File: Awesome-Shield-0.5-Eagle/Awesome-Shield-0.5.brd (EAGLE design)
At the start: 100 x 80 mm, 24 parts, among them J1 ARDUINO_R3_SHIELDUNO_R3_SHIEL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, SW1 SPST_TACT-EVQQ2

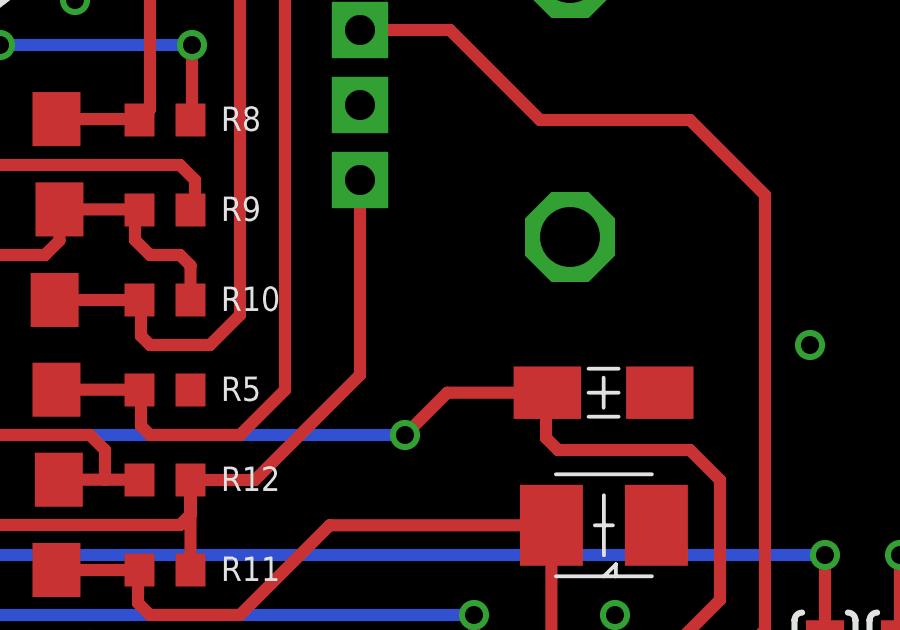
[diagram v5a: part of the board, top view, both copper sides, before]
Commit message: changed vias to round
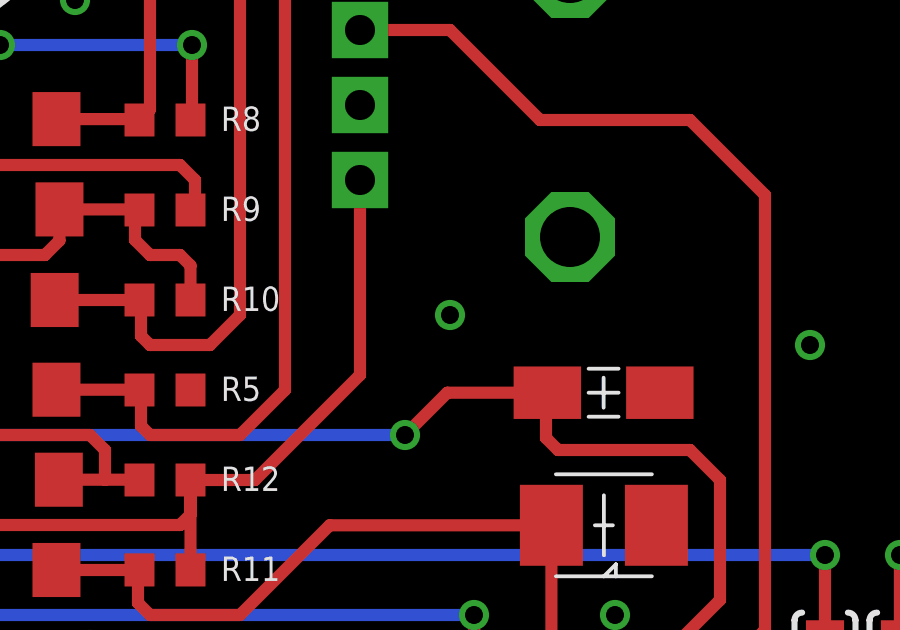
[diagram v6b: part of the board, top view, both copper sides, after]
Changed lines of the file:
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@@
 <vertex x="81.3" y="71.1"/>
 </polygon>
-<via x="32.5" y="57" extent="1-16" drill="0.6" shape="square"/>
-<via x="78.5" y="35.5" extent="1-16" drill="0.6" shape="square"/>
-<via x="38.5" y="21.5" extent="1-16" drill="0.6" shape="square"/>
-<via x="54" y="47" extent="1-16" drill="0.6" shape="square"/>
-<via x="82" y="52.5" extent="1-16" drill="0.6" shape="square"/>
-<via x="72" y="26.5" extent="1-16" drill="0.6" shape="square"/>
-<wire x1="73.495" y1="33.91" x2="73.38" y2="29.49" width="0" layer="19" extent="1-1"/>
+<via x="32.5" y="57" extent="1-16" drill="0.6"/>
+<via x="78.5" y="35.5" extent="1-16" drill="0.6"/>
+<via x="38.5" y="21.5" extent="1-16" drill="0.6"/>
+<via x="54" y="47" extent="1-16" drill="0.6"/>
+<via x="82" y="52.5" extent="1-16" drill="0.6"/>
+<via x="72" y="26.5" extent="1-16" drill="0.6"/>
+<via x="66.5" y="36.5" extent="1-16" drill="0.6"/>
 </signal>
 <signal name="A2">
@@
 <wire x1="69.745" y1="33.91" x2="66.41" y2="33.91" width="0.4064" layer="1"/>
 <wire x1="66.41" y1="33.91" x2="65" y2="32.5" width="0.4064" layer="1"/>
-<via x="65" y="32.5" extent="1-16" drill="0.6" shape="square"/>
+<via x="65" y="32.5" extent="1-16" drill="0.6"/>
 <wire x1="65" y1="32.5" x2="48" y2="32.5" width="0.4064" layer="16"/>
-<via x="48" y="32.5" extent="1-16" drill="0.6" shape="square"/>
+<via x="48" y="32.5" extent="1-16" drill="0.6"/>
 <wire x1="48" y1="32.5" x2="54.5" y2="32.5" width="0.4064" layer="1"/>
 <wire x1="54.5" y1="32.5" x2="55" y2="32" width="0.4064" layer="1"/>
@@
 <wire x1="54.61" y1="20.066" x2="54.61" y2="25.39" width="0.4064" layer="1"/>
 <wire x1="54.61" y1="25.39" x2="54.5" y2="25.5" width="0.4064" layer="1"/>
-<via x="54.5" y="25.5" extent="1-16" drill="0.6" shape="square"/>
+<via x="54.5" y="25.5" extent="1-16" drill="0.6"/>
 <wire x1="54.5" y1="25.5" x2="41" y2="25.5" width="0.4064" layer="16"/>
 <wire x1="41" y1="25.5" x2="38" y2="28.5" width="0.4064" layer="16"/>
-<via x="38" y="28.5" extent="1-16" drill="0.6" shape="square"/>
+<via x="38" y="28.5" extent="1-16" drill="0.6"/>
 <wire x1="38" y1="28.5" x2="34.12" y2="28.5" width="0.4064" layer="1"/>
 <wire x1="34.12" y1="28.5" x2="34.06" y2="28.44" width="0.4064" layer="1"/>
@@
 <wire x1="67.31" y1="20.066" x2="67.31" y2="26.49" width="0.4064" layer="1"/>
 <wire x1="67.31" y1="26.49" x2="67.3" y2="26.5" width="0.4064" layer="1"/>
-<via x="67.3" y="26.5" extent="1-16" drill="0.6" shape="square"/>
+<via x="67.3" y="26.5" extent="1-16" drill="0.6"/>
 <wire x1="67.3" y1="26.5" x2="46.5" y2="26.5" width="0.4064" layer="16"/>
 <wire x1="46.5" y1="26.5" x2="46" y2="27" width="0.4064" layer="16"/>
-<via x="46" y="27" extent="1-16" drill="0.6" shape="square"/>
+<via x="46" y="27" extent="1-16" drill="0.6"/>
 <wire x1="46" y1="27" x2="46" y2="28.5" width="0.4064" layer="1"/>
 <wire x1="46" y1="28.5" x2="39.5" y2="35" width="0.4064" layer="1"/>
@@
 <contactref element="SJ2" pad="1"/>
 <wire x1="81.5" y1="26.008" x2="81.5" y2="28.5" width="0.4064" layer="1"/>
-<via x="81.5" y="28.5" extent="1-16" drill="0.6" shape="square"/>
+<via x="81.5" y="28.5" extent="1-16" drill="0.6"/>
 <wire x1="80" y1="24.5" x2="38" y2="24.5" width="0.4064" layer="16"/>
-<via x="38" y="24.5" extent="1-16" drill="0.6" shape="square"/>
+<via x="38" y="24.5" extent="1-16" drill="0.6"/>
 <wire x1="38" y1="24.5" x2="34.12" y2="24.5" width="0.4064" layer="1"/>
 <wire x1="34.12" y1="24.5" x2="34.06" y2="24.44" width="0.4064" layer="1"/>
@@
 <contactref element="SJ1" pad="1"/>
 <wire x1="79" y1="26.008" x2="79" y2="28.5" width="0.4064" layer="1"/>
-<via x="79" y="28.5" extent="1-16" drill="0.6" shape="square"/>
+<via x="79" y="28.5" extent="1-16" drill="0.6"/>
 <wire x1="79" y1="28.5" x2="42.5" y2="28.5" width="0.4064" layer="16"/>
-<via x="42.5" y="28.5" extent="1-16" drill="0.6" shape="square"/>
+<via x="42.5" y="28.5" extent="1-16" drill="0.6"/>
 <wire x1="42.5" y1="28.5" x2="40.5" y2="28.5" width="0.4064" layer="1"/>
 <wire x1="40.5" y1="28.5" x2="38.5" y2="26.5" width="0.4064" layer="1"/>
@@
 <wire x1="69.85" y1="68.58" x2="69.85" y2="66.15" width="0.4064" layer="1"/>
 <wire x1="69.85" y1="66.15" x2="70.5" y2="65.5" width="0.4064" layer="1"/>
-<via x="70.5" y="65.5" extent="1-16" drill="0.6" shape="square"/>
+<via x="70.5" y="65.5" extent="1-16" drill="0.6"/>
 <wire x1="70.5" y1="65.5" x2="61" y2="65.5" width="0.4064" layer="16"/>
 <wire x1="61" y1="65.5" x2="37.3" y2="41.8" width="0.4064" layer="16"/>
-<via x="37.3" y="41.8" extent="1-16" drill="0.6" shape="square"/>
+<via x="37.3" y="41.8" extent="1-16" drill="0.6"/>
 <wire x1="37.3" y1="41.8" x2="34.14" y2="41.8" width="0.4064" layer="1"/>
 <wire x1="34.14" y1="41.8" x2="34.06" y2="41.72" width="0.4064" layer="1"/>
@@
 <wire x1="50.538" y1="43.03" x2="50.538" y2="44.538" width="0.4064" layer="1"/>
 <wire x1="50.538" y1="44.538" x2="51.5" y2="45.5" width="0.4064" layer="1"/>
-<via x="51.5" y="45.5" extent="1-16" drill="0.6" shape="square"/>
+<via x="51.5" y="45.5" extent="1-16" drill="0.6"/>
 <wire x1="51.5" y1="45.5" x2="57.9" y2="45.5" width="0.4064" layer="16"/>
-<via x="57.9" y="45.5" extent="1-16" drill="0.6" shape="square"/>
+<via x="57.9" y="45.5" extent="1-16" drill="0.6"/>
 <wire x1="57.9" y1="45.5" x2="57.9" y2="43.05" width="0.4064" layer="1"/>
 <wire x1="57.9" y1="43.05" x2="57.85" y2="43" width="0.4064" layer="1"/>

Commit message: powered potentiometer from IOREF instead of +3V3 power rail, trace tweaks
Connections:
- new net IOREF: J1.IOREF, RV1.P$3
- net +3V3: no longer RV1.P$3
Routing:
- net IOREF: track 0.00 -> 40.0 mm, vias 0 -> 2
- net +3V3: track 36.6 -> 23.0 mm
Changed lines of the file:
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@@
 <contactref element="R6" pad="1"/>
 <contactref element="R7" pad="2"/>
-<contactref element="RV1" pad="P$3"/>
 <contactref element="R12" pad="2"/>
 <contactref element="R11" pad="2"/>
@@
 <wire x1="57.85" y1="29.85" x2="57.5" y2="29.5" width="0.4064" layer="1"/>
 <wire x1="57.5" y1="29.5" x2="50.538" y2="29.5" width="0.4064" layer="1"/>
-<wire x1="63.5" y1="41" x2="63.5" y2="34.5" width="0.4064" layer="1"/>
-<wire x1="63.5" y1="34.5" x2="60" y2="31" width="0.4064" layer="1"/>
-<wire x1="60" y1="31" x2="57.85" y2="31" width="0.4064" layer="1"/>
 </signal>
 <signal name="A1">
@@
 <wire x1="69.5" y1="43" x2="66.5" y2="46" width="0.4064" layer="1"/>
 </signal>
+<signal name="IOREF">
+<contactref element="J1" pad="IOREF"/>
+<contactref element="RV1" pad="P$3"/>
+<wire x1="63.5" y1="41" x2="63.5" y2="35" width="0.4064" layer="1"/>
+<via x="63.5" y="35" extent="1-16" drill="0.6"/>
+<wire x1="63.5" y1="35" x2="46.5" y2="35" width="0.4064" layer="16"/>
+<wire x1="46.5" y1="35" x2="45" y2="33.5" width="0.4064" layer="16"/>
+<via x="45" y="33.5" extent="1-16" drill="0.6"/>
+<wire x1="45" y1="33.5" x2="45" y2="32" width="0.4064" layer="1"/>
+<wire x1="45" y1="32" x2="48" y2="29" width="0.4064" layer="1"/>
+<wire x1="48" y1="29" x2="48" y2="25" width="0.4064" layer="1"/>
+<wire x1="48" y1="25" x2="47" y2="24" width="0.4064" layer="1"/>
+<wire x1="47" y1="24" x2="47" y2="20.33" width="0.4064" layer="1"/>
+<wire x1="47" y1="20.33" x2="46.99" y2="20.32" width="0.4064" layer="1"/>
+</signal>
 </signals>

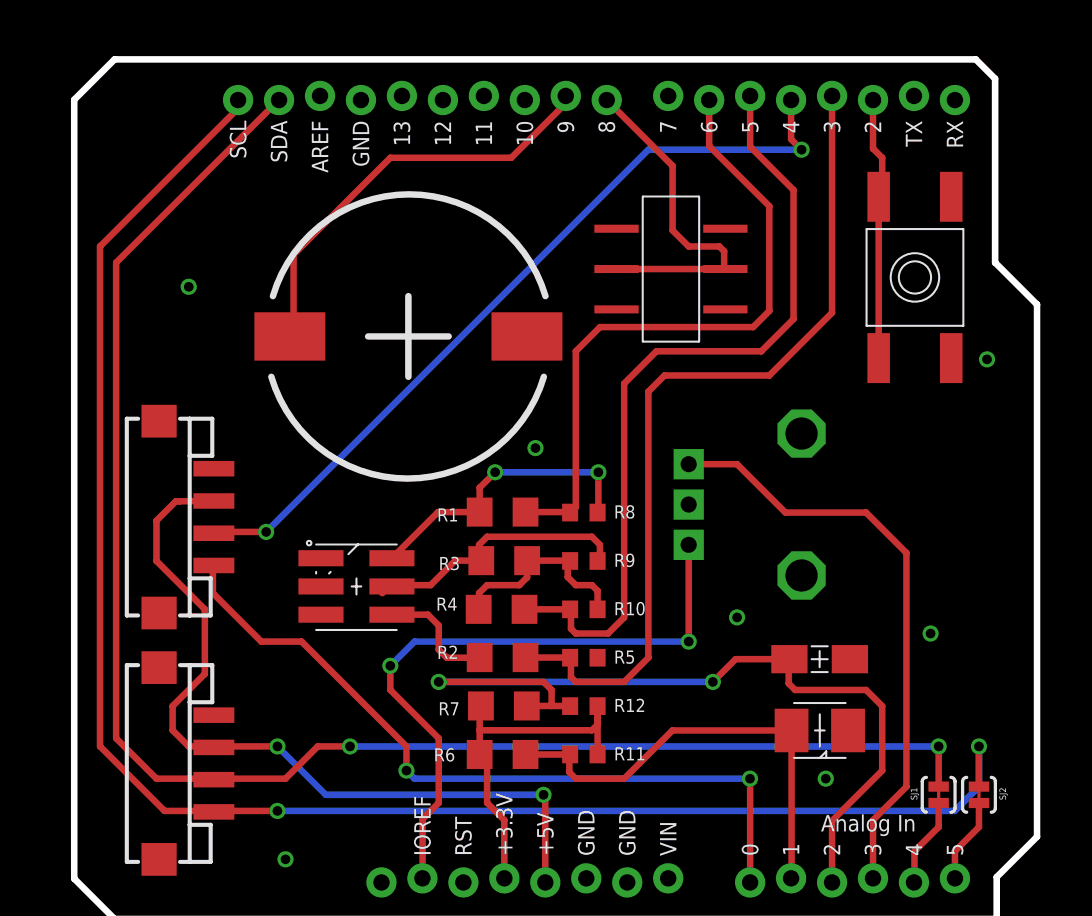
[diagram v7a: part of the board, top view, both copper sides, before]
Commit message: removed redundant vias, trace tweaks
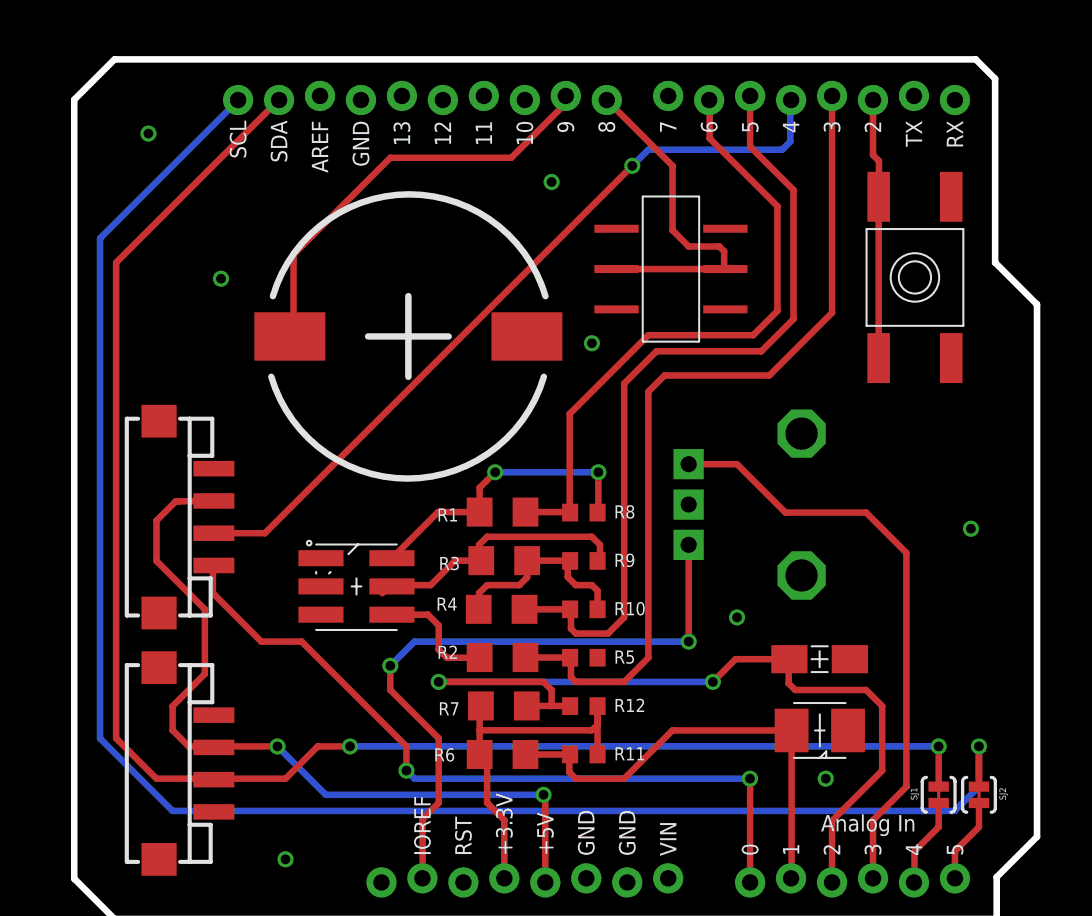
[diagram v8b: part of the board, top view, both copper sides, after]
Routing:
- net D4: track 49.6 -> 48.4 mm, vias 2 -> 1
- net D6: track 40.3 -> 39.2 mm
- net SCL: track 105.4 -> 105.3 mm, vias 2 -> 1
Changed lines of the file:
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@@
 <vertex x="81.3" y="71.1"/>
 </polygon>
-<via x="32.5" y="57" extent="1-16" drill="0.6"/>
-<via x="78.5" y="35.5" extent="1-16" drill="0.6"/>
+<via x="34.5" y="57.5" extent="1-16" drill="0.6"/>
+<via x="81" y="42" extent="1-16" drill="0.6"/>
 <via x="38.5" y="21.5" extent="1-16" drill="0.6"/>
-<via x="54" y="47" extent="1-16" drill="0.6"/>
-<via x="82" y="52.5" extent="1-16" drill="0.6"/>
+<via x="57.5" y="53.5" extent="1-16" drill="0.6"/>
+<via x="55" y="63.5" extent="1-16" drill="0.6"/>
 <via x="72" y="26.5" extent="1-16" drill="0.6"/>
 <via x="66.5" y="36.5" extent="1-16" drill="0.6"/>
+<via x="30" y="66.5" extent="1-16" drill="0.6"/>
 </signal>
 <signal name="A2">
@@
 <contactref element="SW1" pad="B'"/>
 <contactref element="J1" pad="D2"/>
-<wire x1="74.93" y1="68.58" x2="74.93" y2="65.57" width="0.4064" layer="1"/>
-<wire x1="74.93" y1="65.57" x2="75.5" y2="65" width="0.4064" layer="1"/>
-<wire x1="75.5" y1="65" x2="75.5" y2="62.8" width="0.4064" layer="1"/>
+<wire x1="74.93" y1="68.58" x2="74.93" y2="65.17" width="0.4064" layer="1"/>
 <wire x1="75.5" y1="62.8" x2="75.28" y2="62.58" width="0.4064" layer="1"/>
 <wire x1="75.28" y1="62.58" x2="75.28" y2="52.58" width="0.4064" layer="1"/>
+<wire x1="74.93" y1="65.17" x2="75.3" y2="64.8" width="0.4064" layer="1"/>
+<wire x1="75.3" y1="64.8" x2="75.3" y2="62.6" width="0.4064" layer="1"/>
+<wire x1="75.3" y1="62.6" x2="75.28" y2="62.58" width="0.4064" layer="1"/>
 </signal>
 <signal name="D6">
@@
 <wire x1="53.382" y1="43.03" x2="56.12" y2="43.03" width="0.4064" layer="1"/>
 <wire x1="56.12" y1="43.03" x2="56.15" y2="43" width="0.4064" layer="1"/>
-<wire x1="56.5" y1="53" x2="56.5" y2="43.35" width="0.4064" layer="1"/>
-<wire x1="56.5" y1="43.35" x2="56.15" y2="43" width="0.4064" layer="1"/>
-<wire x1="64.77" y1="68.27" x2="64.77" y2="65.73" width="0.4064" layer="1"/>
-<wire x1="64.77" y1="65.73" x2="68.5" y2="62" width="0.4064" layer="1"/>
-<wire x1="68.5" y1="62" x2="68.5" y2="55.5" width="0.4064" layer="1"/>
-<wire x1="68.5" y1="55.5" x2="67.5" y2="54.5" width="0.4064" layer="1"/>
-<wire x1="67.5" y1="54.5" x2="58" y2="54.5" width="0.4064" layer="1"/>
-<wire x1="58" y1="54.5" x2="56.5" y2="53" width="0.4064" layer="1"/>
-<wire x1="64.77" y1="68.27" x2="64.77" y2="68.58" width="0" layer="19" extent="1-1"/>
+<wire x1="56.12" y1="43.03" x2="56.12" y2="49.12" width="0.4064" layer="1"/>
+<wire x1="56.12" y1="49.12" x2="61" y2="54" width="0.4064" layer="1"/>
+<wire x1="61" y1="54" x2="67.5" y2="54" width="0.4064" layer="1"/>
+<wire x1="67.5" y1="54" x2="69" y2="55.5" width="0.4064" layer="1"/>
+<wire x1="69" y1="55.5" x2="69" y2="62" width="0.4064" layer="1"/>
+<wire x1="69" y1="62" x2="64.8" y2="66.2" width="0.4064" layer="1"/>
+<wire x1="64.8" y1="66.2" x2="64.8" y2="68.55" width="0.4064" layer="1"/>
+<wire x1="64.8" y1="68.55" x2="64.77" y2="68.58" width="0.4064" layer="1"/>
 </signal>
 <signal name="+5V">
@@
 <wire x1="81.5" y1="26.008" x2="81.5" y2="28.5" width="0.4064" layer="1"/>
 <via x="81.5" y="28.5" extent="1-16" drill="0.6"/>
-<wire x1="80" y1="24.5" x2="38" y2="24.5" width="0.4064" layer="16"/>
-<via x="38" y="24.5" extent="1-16" drill="0.6"/>
-<wire x1="38" y1="24.5" x2="34.12" y2="24.5" width="0.4064" layer="1"/>
+<wire x1="80" y1="24.5" x2="31.5" y2="24.5" width="0.4064" layer="16"/>
 <wire x1="34.12" y1="24.5" x2="34.06" y2="24.44" width="0.4064" layer="1"/>
-<wire x1="35.56" y1="68.58" x2="35.56" y2="68.06" width="0.4064" layer="1"/>
-<wire x1="35.56" y1="68.06" x2="27" y2="59.5" width="0.4064" layer="1"/>
-<wire x1="27" y1="59.5" x2="27" y2="28.5" width="0.4064" layer="1"/>
-<wire x1="27" y1="28.5" x2="31" y2="24.5" width="0.4064" layer="1"/>
-<wire x1="31" y1="24.5" x2="34" y2="24.5" width="0.4064" layer="1"/>
 <wire x1="34" y1="24.5" x2="34.06" y2="24.44" width="0.4064" layer="1"/>
 <wire x1="80" y1="24.5" x2="80" y2="24.508" width="0.4064" layer="16"/>
 <wire x1="80" y1="24.508" x2="81.5" y2="26.008" width="0.4064" layer="16"/>
 <wire x1="81.5" y1="26.008" x2="81.5" y2="28.5" width="0.4064" layer="16"/>
+<wire x1="35.56" y1="68.58" x2="35.56" y2="68.56" width="0.4064" layer="16"/>
+<wire x1="35.56" y1="68.56" x2="27" y2="60" width="0.4064" layer="16"/>
+<wire x1="27" y1="60" x2="27" y2="29" width="0.4064" layer="16"/>
+<wire x1="27" y1="29" x2="31.5" y2="24.5" width="0.4064" layer="16"/>
+<wire x1="31.5" y1="24.5" x2="34" y2="24.5" width="0" layer="19" extent="1-16"/>
 </signal>
 <signal name="SDA">
@@
 <contactref element="J1" pad="D4"/>
 <contactref element="J2" pad="2"/>
-<wire x1="69.85" y1="68.58" x2="69.85" y2="66.15" width="0.4064" layer="1"/>
-<wire x1="69.85" y1="66.15" x2="70.5" y2="65.5" width="0.4064" layer="1"/>
-<via x="70.5" y="65.5" extent="1-16" drill="0.6"/>
-<wire x1="70.5" y1="65.5" x2="61" y2="65.5" width="0.4064" layer="16"/>
-<wire x1="61" y1="65.5" x2="37.3" y2="41.8" width="0.4064" layer="16"/>
-<via x="37.3" y="41.8" extent="1-16" drill="0.6"/>
-<wire x1="37.3" y1="41.8" x2="34.14" y2="41.8" width="0.4064" layer="1"/>
-<wire x1="34.14" y1="41.8" x2="34.06" y2="41.72" width="0.4064" layer="1"/>
+<wire x1="34.06" y1="41.72" x2="37.22" y2="41.72" width="0.4064" layer="1"/>
+<wire x1="37.22" y1="41.72" x2="60" y2="64.5" width="0.4064" layer="1"/>
+<via x="60" y="64.5" extent="1-16" drill="0.6"/>
+<wire x1="60" y1="64.5" x2="61" y2="65.5" width="0.4064" layer="16"/>
+<wire x1="61" y1="65.5" x2="69.3" y2="65.5" width="0.4064" layer="16"/>
+<wire x1="69.3" y1="65.5" x2="69.8" y2="66" width="0.4064" layer="16"/>
+<wire x1="69.8" y1="66" x2="69.8" y2="68.53" width="0.4064" layer="16"/>
+<wire x1="69.8" y1="68.53" x2="69.85" y2="68.58" width="0.4064" layer="16"/>
 </signal>
 <signal name="N$2">
